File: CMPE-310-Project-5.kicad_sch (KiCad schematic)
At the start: 5 parts, among them J1 DSUB-9, U1 max235cpg, U3 pkd8279, U4 8086_Min_Mode

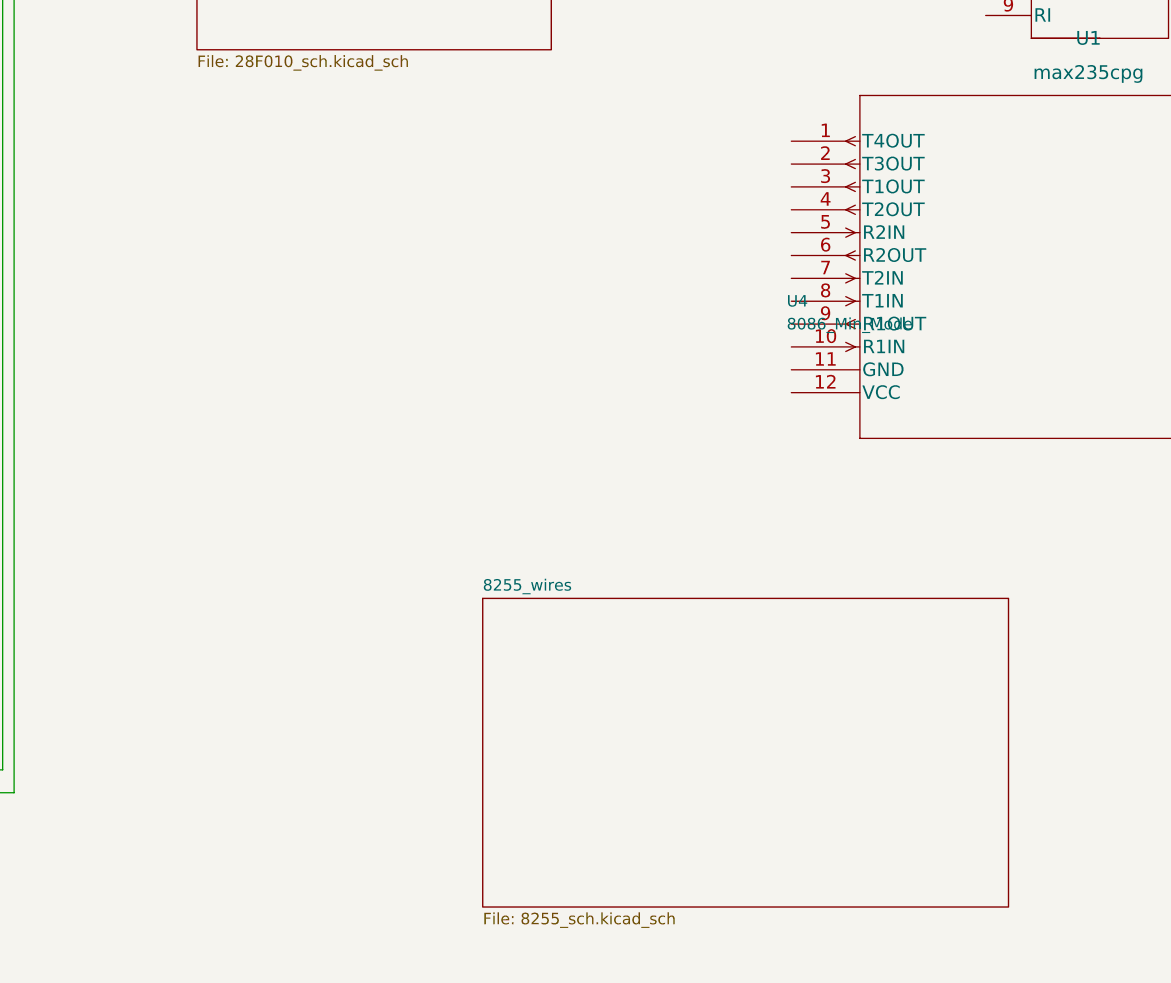
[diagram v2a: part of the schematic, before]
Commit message: Added new schematic sheets for INTR components
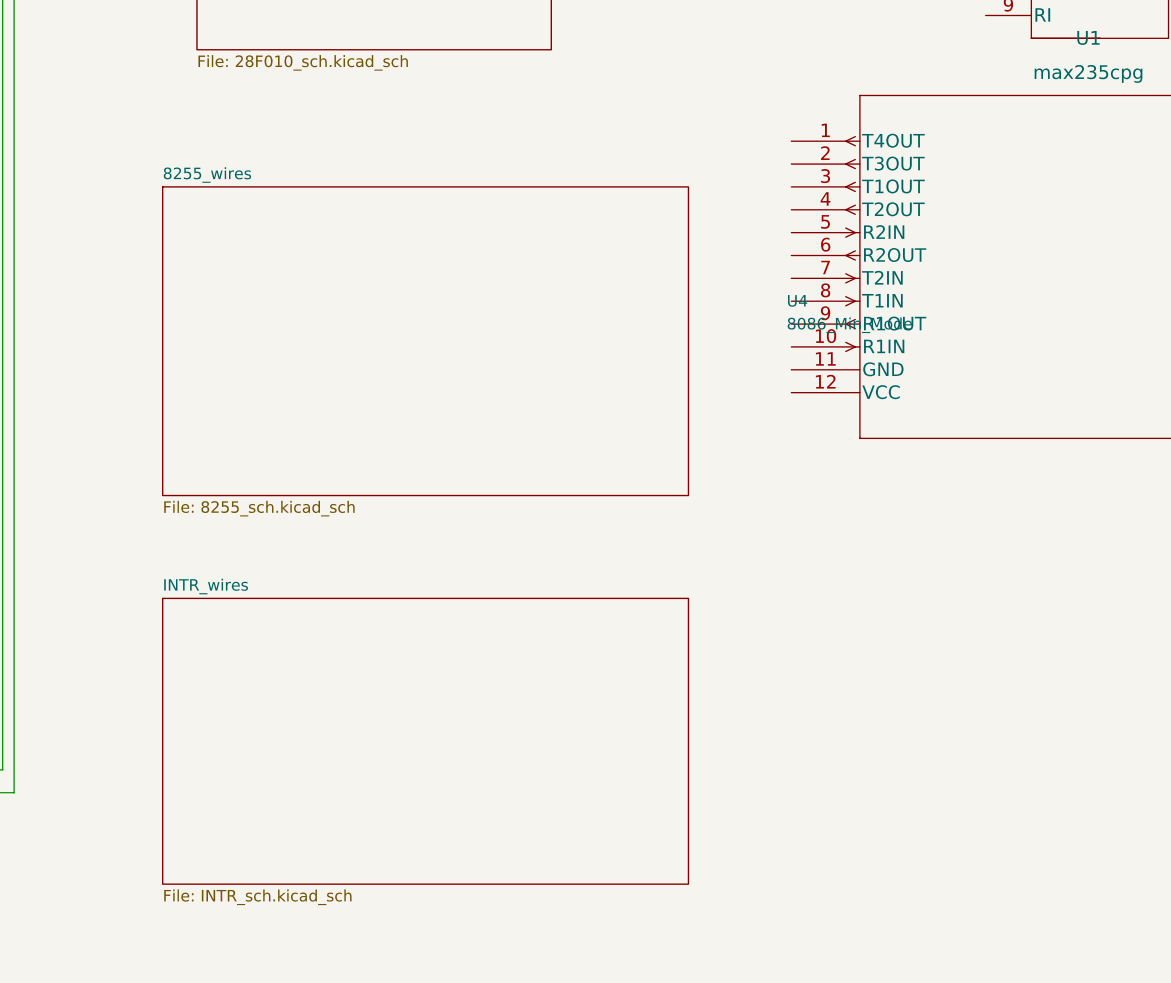
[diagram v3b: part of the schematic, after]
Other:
- added sheet INTR_wires (INTR_sch.kicad_sch)
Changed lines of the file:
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@@
     (pin "9")
   )
-  (sheet (at 133.35 115.57) (size 58.42 34.29) (fields_autoplaced)
+  (sheet (at 97.79 69.85) (size 58.42 34.29) (fields_autoplaced)
     (stroke (width 0.1524) (type solid) (color 0 0 0 0))
     (fill (color 0 0 0 0.0000))
-    (property "Sheet name" "8255_wires" (id 0) (at 133.35 114.8584 0)
+    (property "Sheet name" "8255_wires" (id 0) (at 97.79 69.1384 0)
       (effects (font (size 1.27 1.27)) (justify left bottom))
     )
-    (property "Sheet file" "8255_sch.kicad_sch" (id 1) (at 133.35 150.4446 0)
+    (property "Sheet file" "8255_sch.kicad_sch" (id 1) (at 97.79 104.7246 0)
+      (effects (font (size 1.27 1.27)) (justify left top))
+    )
+  )
+  (sheet (at 97.79 115.57) (size 58.42 31.75) (fields_autoplaced)
+    (stroke (width 0.1524) (type solid) (color 0 0 0 0))
+    (fill (color 0 0 0 0.0000))
+    (property "Sheet name" "INTR_wires" (id 0) (at 97.79 114.8584 0)
+      (effects (font (size 1.27 1.27)) (justify left bottom))
+    )
+    (property "Sheet file" "INTR_sch.kicad_sch" (id 1) (at 97.79 147.9046 0)
       (effects (font (size 1.27 1.27)) (justify left top))
     )
@@
     (path "/cce1404b-fc30-47cc-b852-e0061990f2bb" (page "2"))
     (path "/65a0be0e-e533-4531-a6d7-d67f7f67ab34" (page "3"))
+    (path "/87af81b5-cad9-406d-8283-65af2b602860" (page "4"))
+    (path "/87af81b5-cad9-406d-8283-65af2b602860/4f164966-96b4-4af1-b000-64fc7501cfa0" (page "5"))
   )
   (symbol_instances
@@
       (reference "U17") (unit 1) (value "CY7C199") (footprint "")
     )
+    (path "/87af81b5-cad9-406d-8283-65af2b602860/4f164966-96b4-4af1-b000-64fc7501cfa0/059acf37-76a9-40b1-bb25-35aaece591a3"
+      (reference "U?") (unit 1) (value "16550") (footprint "Package_DIP:DIP-40_W15.24mm")
+    )
+    (path "/87af81b5-cad9-406d-8283-65af2b602860/72504f11-f169-4f76-9103-8f0a4cac0355"
+      (reference "U?") (unit 1) (value "8259A") (footprint "Package_DIP:DIP-28_W15.24mm")
+    )
   )

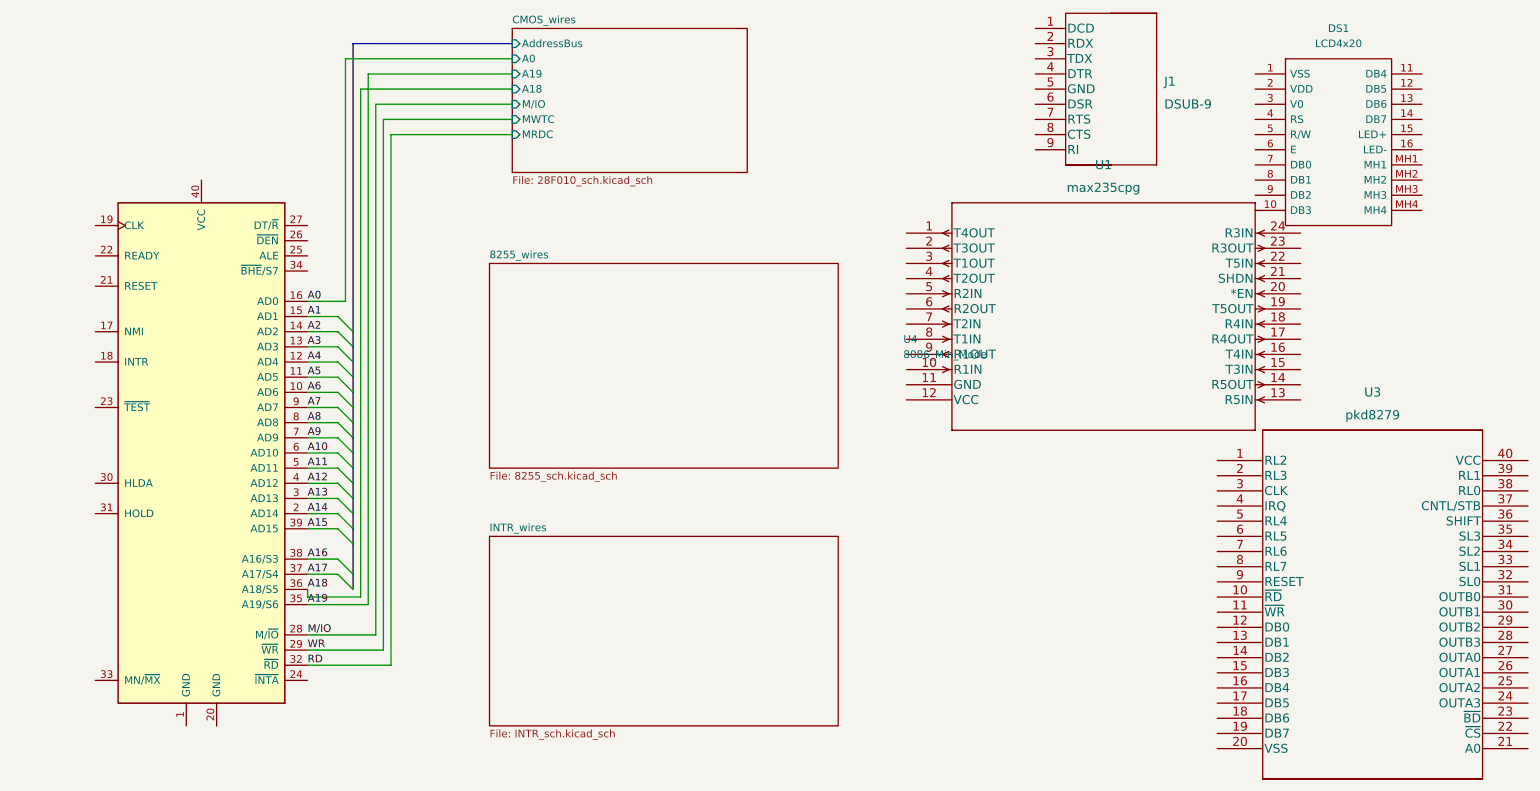
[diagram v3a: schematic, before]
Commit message: Wired the UART to the 8259A
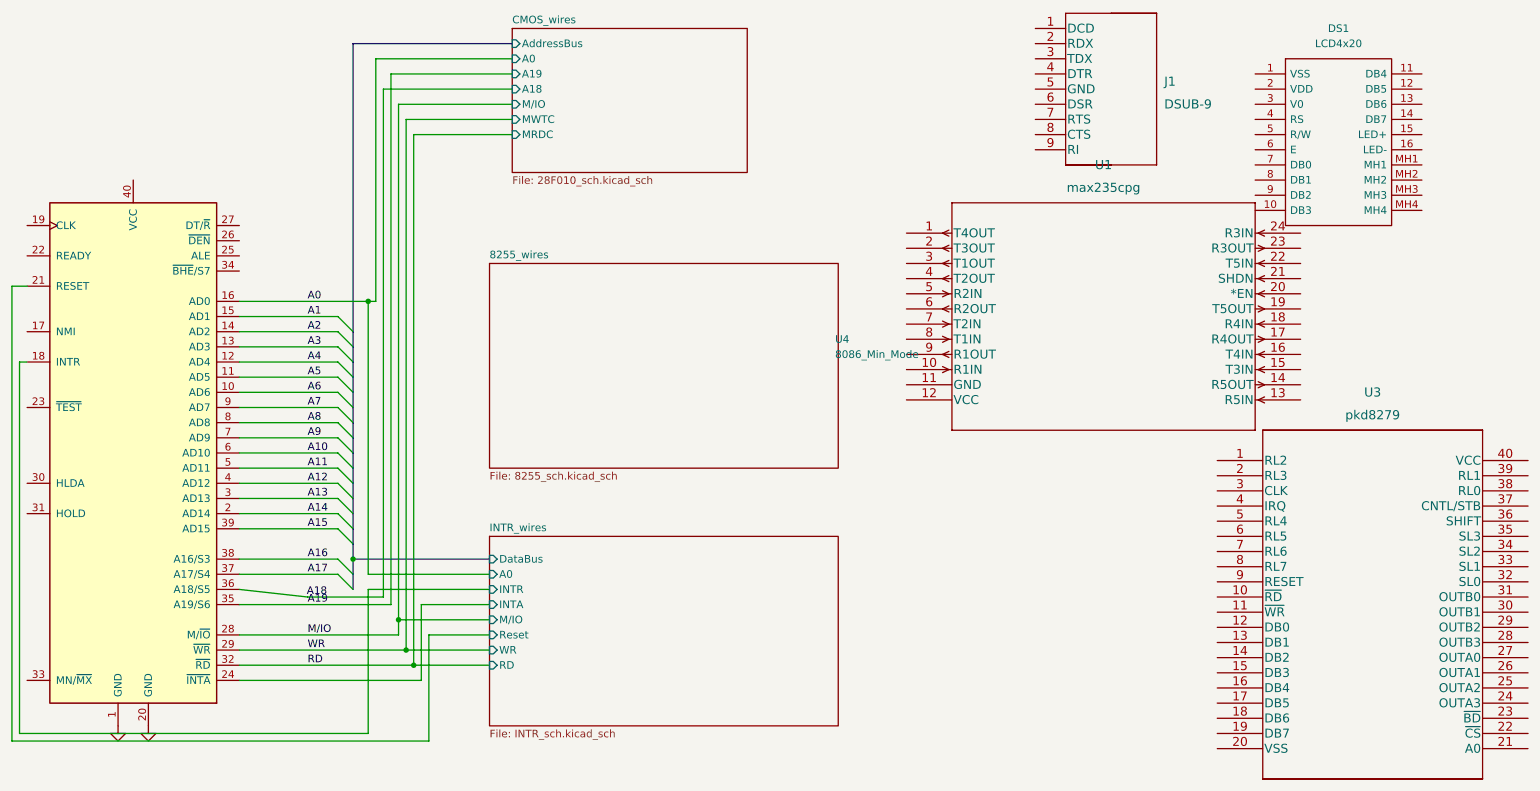
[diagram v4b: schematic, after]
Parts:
- DS1: footprint LCD4x20 -> (none)
- J1: footprint DSUB-9 -> (none)
- U1: footprint max235cpg -> (none)
- U3: footprint pkd8279 -> (none)
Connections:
- net GND: now reaches U4.1 (GND)
- net GND: now also U4.20 (GND)
- net INTR_wires/INTR: now reaches U4.18 (INTR)
- net INTR_wires/Reset: now reaches U4.21 (RESET)
- net INTR_wires/INTA: now reaches U4.24 (~{INTA})
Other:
- sheet INTR_wires ports: added A0, DataBus, INTA, INTR, M/IO, RD, Reset, WR; removed none
- moved on the sheet: U4

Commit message: Wired up Decoding of 8255s, 8254, and 8279
Also fixed up the decoding for the 16550 and the 8259 as well as labeled all wires into/from the bus.
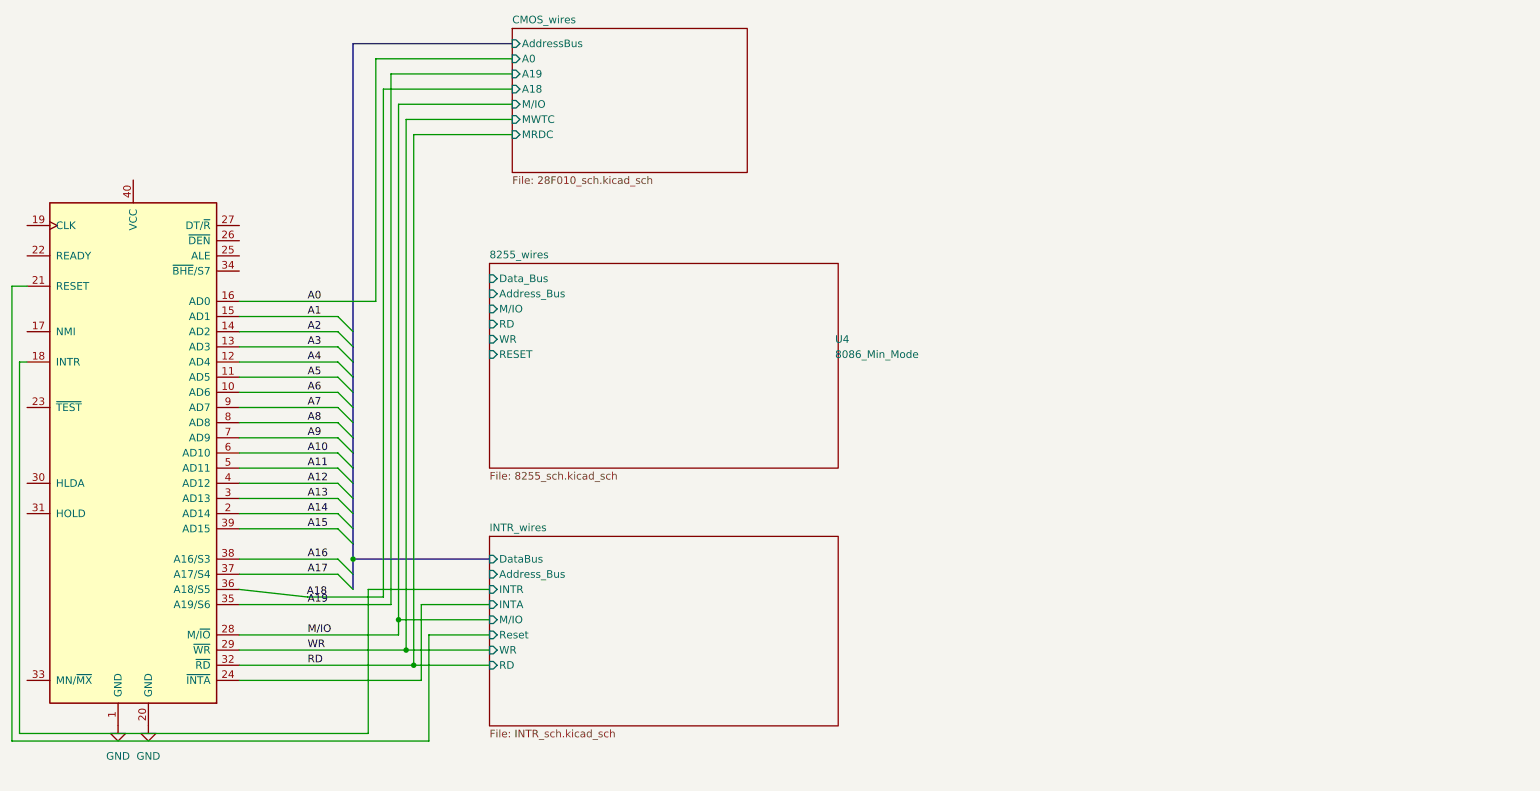
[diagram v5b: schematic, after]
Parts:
- removed DS1: LCD4x20, symbol LCD4x20:LCD4x20
- removed J1: DSUB-9, symbol DSUB-9:DSUB-9
- removed U1: max235cpg, symbol max235cpg:max235cpg
- removed U3: pkd8279, symbol pkd8279:pkd8279
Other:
- sheet 8255_wires ports: added Address_Bus, Data_Bus, M/IO, RD, RESET, WR; removed none
- sheet INTR_wires ports: added Address_Bus; removed A0

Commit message: Wired the max235 and DSUB9
We will double check the wiring tomorrow. Also added the data bus
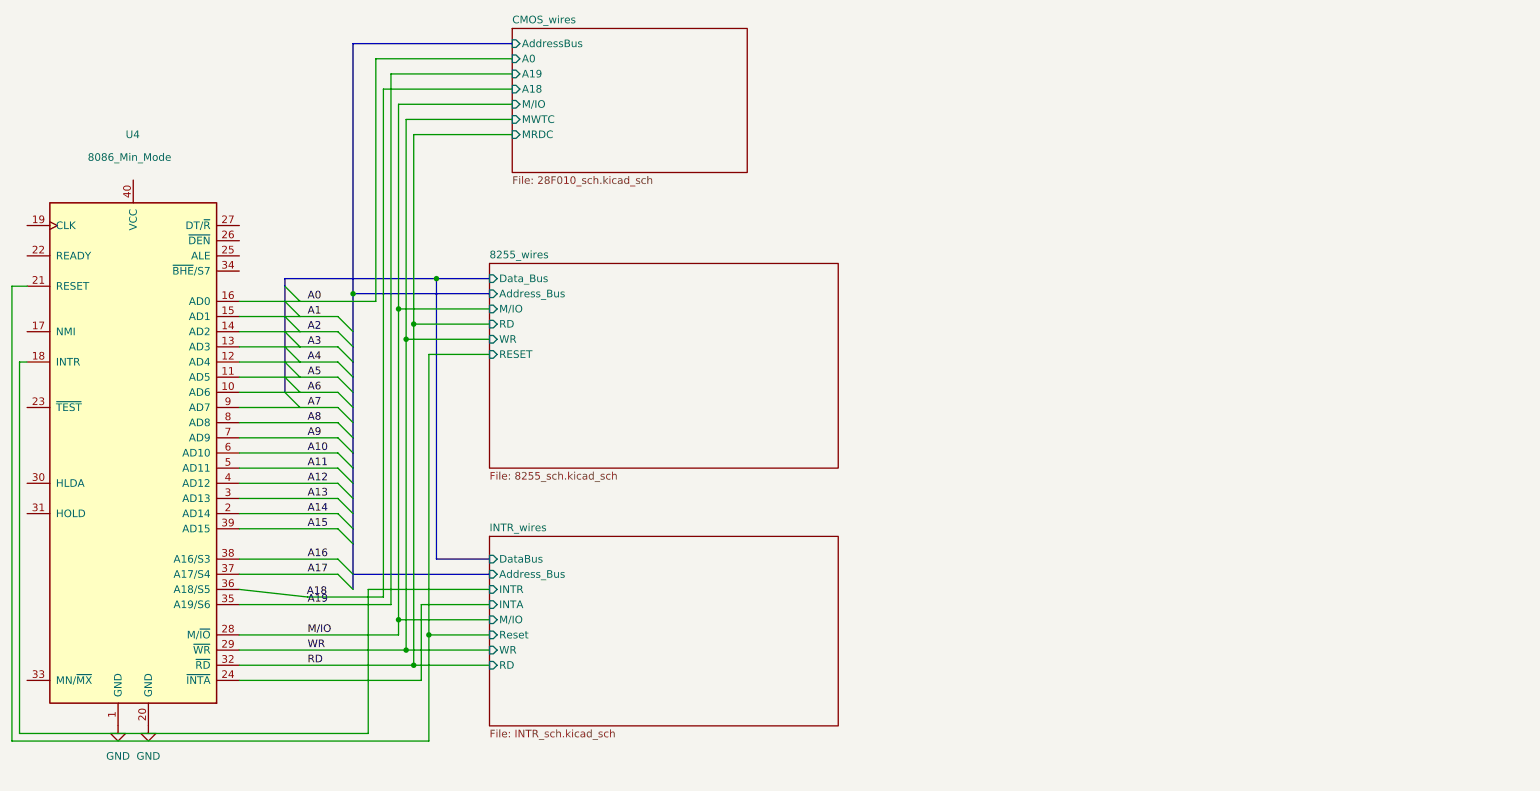
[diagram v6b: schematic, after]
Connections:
- net INTR_wires/Reset is gone; now on net 8255_wires/RESET: U4.21 (RESET)

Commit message: Added Clock Circuit
Moved the main circuit to the right and added a simple clock generator circuit to the left of the 8086. Still need to wire reset switch
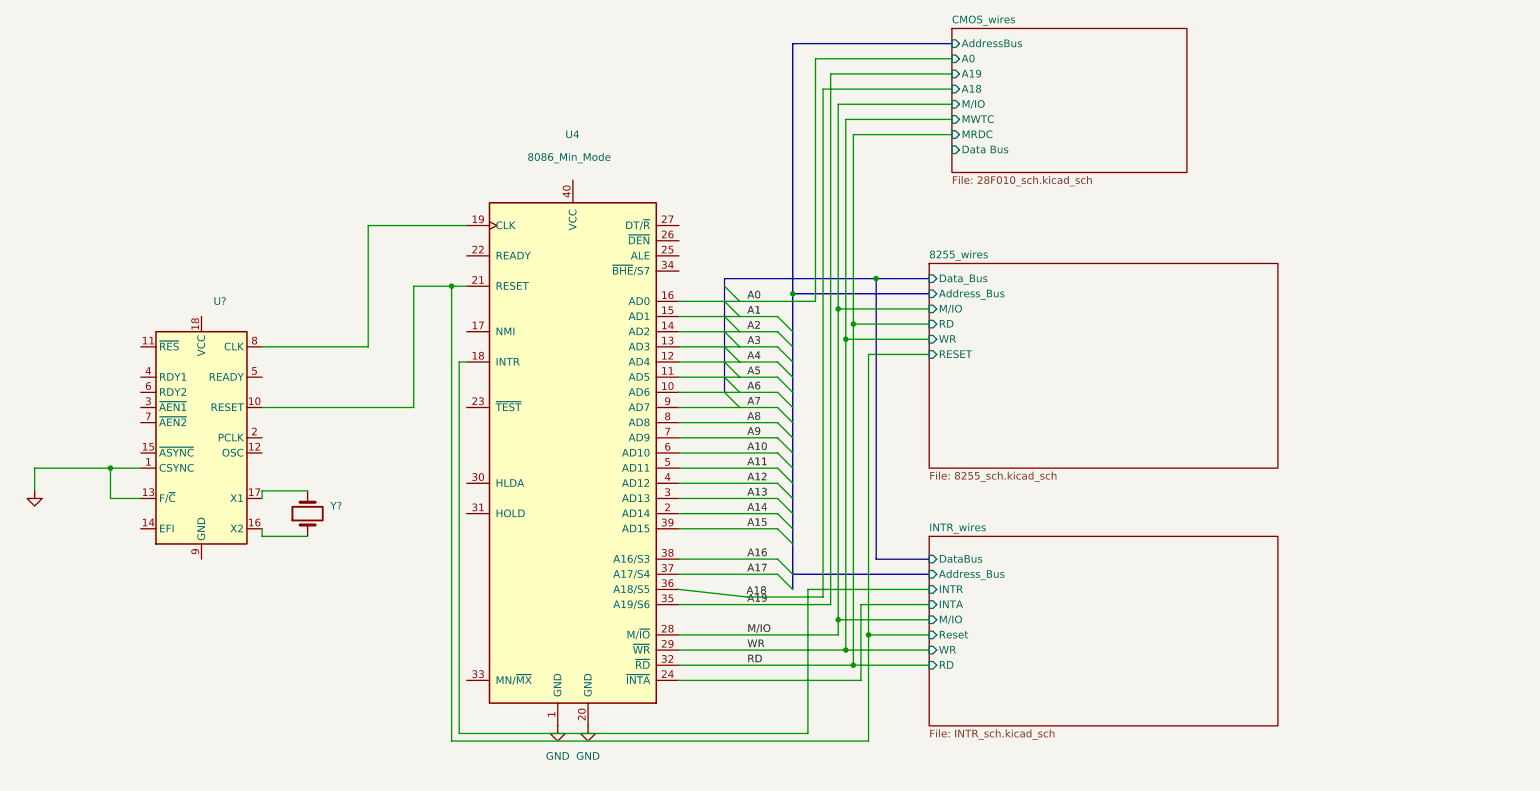
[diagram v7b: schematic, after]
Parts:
- added U?: (no value), symbol Timer:8284
- added Y?: (no value), symbol Device:Crystal
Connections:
- net 8255_wires/RESET: now also U?.10 (RESET)
- net GND: now also U?.1 (CSYNC), U?.13 (F/~{C})
- net at U4.19 (CLK): now also U?.8 (CLK)
- new net: U?.16 (X2), Y?.1
- new net: U?.17 (X1), Y?.2
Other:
- sheet CMOS_wires ports: added Data Bus; removed none
- moved on the sheet: U4

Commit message: Added the databus
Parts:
- U?: value (none) -> 8284; footprint (none) -> Package_DIP:DIP-18_W7.62mm
- Y?: value (none) -> Crystal
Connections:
- net INTR_wires/PCLK: now reaches U?.2 (PCLK)
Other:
- sheet CMOS_wires ports: added DataBus; removed none
- sheet INTR_wires ports: added PCLK; removed none
